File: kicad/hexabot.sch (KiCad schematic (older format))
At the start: 102 parts, among them P1 BATTERY, P10 BUMP2, P11 USB_B, P12 DEBUG, P13 NC, P14 MOTOR_R, P15 MOTOR_L, P16 UART1_5V, P17 ENC1, P18 ENC2, P19 ENC3, P2 EXT_POWER, P20 ENC4, P21 UART2_FTDI3V3, P22 NC, P23 START, P24 DYNAMIXEL2, P25 NC, P26 NC, P27 NC, P3 SERVO1, P4 SERVO2, P5 DYNAMIXEL1, P6 PICKIT, P7 PANIC BUTTON, P8 NC, P9 BUMP1, Q1 Q_NMOS_GSD, Q2 Q_NMOS_GSD, Q3 Q_NMOS_GSD, Q4 Q_NMOS_GSD, SW1 PUSH1, SW2 PUSH2, U1 PTN78020 +5V, U2 PTN78020 SERVO, U3 MCP1727, U4 DSPIC33EP256MU806, Y1 8M

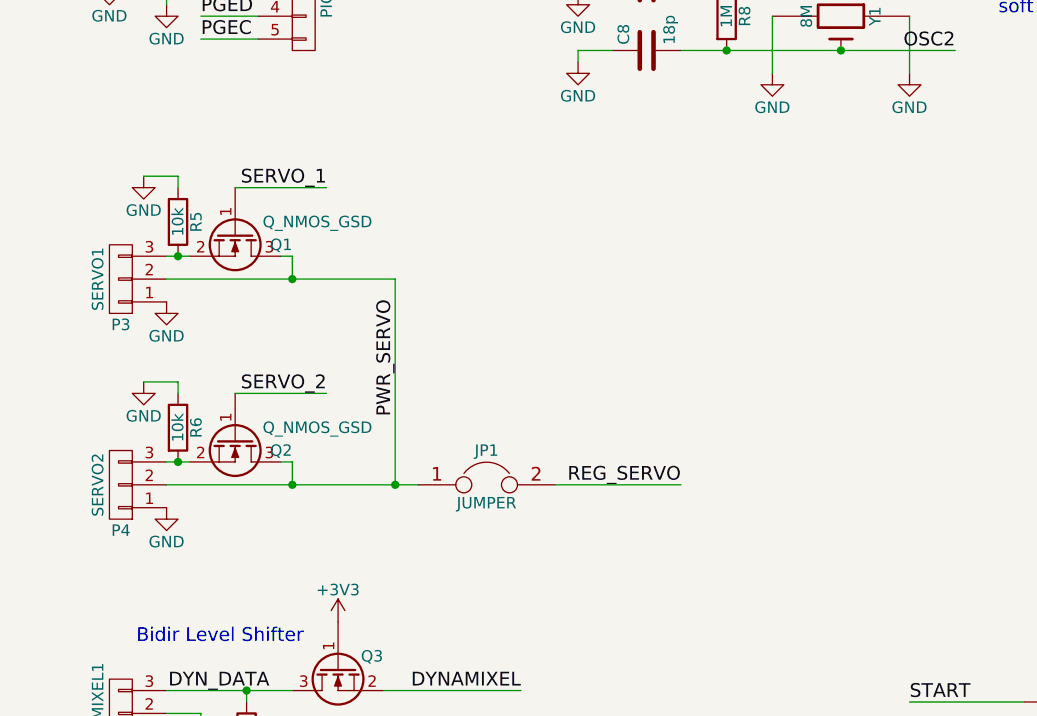
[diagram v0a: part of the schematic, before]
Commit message: Fix servo transistor in schematics, the netlist will have to change
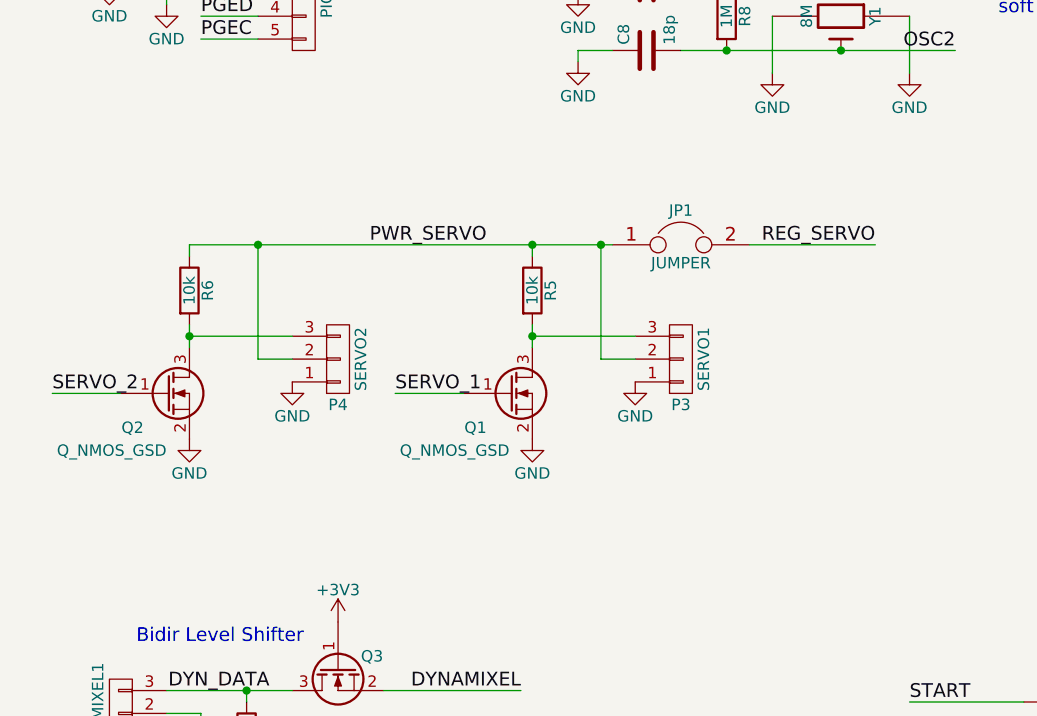
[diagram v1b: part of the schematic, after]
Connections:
- net GND: now also Q1.2 (S), Q2.2 (S); no longer R5.1, R6.1
- net PWR_SERVO: now also R5.1, R6.1; no longer Q1.3 (D), Q2.3 (D)
- net at P3.3 (P3), R5.2: now also Q1.3 (D); no longer Q1.2 (S)
- net at P4.3 (P3), R6.2: now also Q2.3 (D); no longer Q2.2 (S)
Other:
- moved on the sheet: JP1, P3, Q1, R5
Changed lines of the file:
@@
 L CONN_01X03 P3
 U 1 1 55780543
-P 1050 7150
-F 0 "P3" H 1050 7350 50  0000 C CNN
-F 1 "SERVO1" V 1150 7150 50  0000 C CNN
-F 2 "Pin_Headers:Pin_Header_Straight_1x03" H 1050 7150 60  0001 C CNN
-F 3 "" H 1050 7150 60  0000 C CNN
-	1    1050 7150
-	-1   0    0    1
-$EndComp
-Text Label 1950 6750 2    60   ~ 0
+P 3500 7500
+F 0 "P3" H 3500 7700 50  0000 C CNN
+F 1 "SERVO1" V 3600 7500 50  0000 C CNN
+F 2 "Pin_Headers:Pin_Header_Straight_1x03" H 3500 7500 60  0001 C CNN
+F 3 "" H 3500 7500 60  0000 C CNN
+	1    3500 7500
+	1    0    0    1
+$EndComp
+Text Label 2250 7650 0    60   ~ 0
 SERVO_1
 $Comp
 L GND #PWR017
 U 1 1 55781069
-P 1250 7250
-F 0 "#PWR017" H 1250 7000 50  0001 C CNN
-F 1 "GND" H 1250 7100 50  0000 C CNN
-F 2 "" H 1250 7250 60  0000 C CNN
-F 3 "" H 1250 7250 60  0000 C CNN
-	1    1250 7250
-	1    0    0    -1
+P 3300 7600
+F 0 "#PWR017" H 3300 7350 50  0001 C CNN
+F 1 "GND" H 3300 7450 50  0000 C CNN
+F 2 "" H 3300 7600 60  0000 C CNN
+F 3 "" H 3300 7600 60  0000 C CNN
+	1    3300 7600
+	-1   0    0    -1
 $EndComp
 $Comp
 L Q_NMOS_GSD Q1
 U 1 1 55782C1B
-P 1550 6950
-F 0 "Q1" V 1600 7200 50  0000 R CNN
-F 1 "Q_NMOS_GSD" V 1500 7550 50  0000 R CNN
-F 2 "Housings_SOT-23_SOT-143_TSOT-6:SOT-23" H 1750 7050 29  0001 C CNN
-F 3 "" H 1550 6950 60  0000 C CNN
-	1    1550 6950
-	0    1    1    0
+P 2750 7650
+F 0 "Q1" H 2650 7500 50  0000 R CNN
+F 1 "Q_NMOS_GSD" H 2750 7400 50  0000 R CNN
+F 2 "Housings_SOT-23_SOT-143_TSOT-6:SOT-23" H 2950 7750 29  0001 C CNN
+F 3 "" H 2750 7650 60  0000 C CNN
+	1    2750 7650
+	1    0    0    -1
 $EndComp
 Text Label 5750 4150 0    60   ~ 0
@@
 L JUMPER JP1
 U 1 1 55796F00
-P 2650 8050
-F 0 "JP1" H 2650 8200 50  0000 C CNN
-F 1 "JUMPER" H 2650 7970 50  0000 C CNN
-F 2 "Pin_Headers:Pin_Header_Straight_1x02" H 2650 8050 60  0001 C CNN
-F 3 "" H 2650 8050 60  0000 C CNN
-	1    2650 8050
+P 3500 7000
+F 0 "JP1" H 3500 7150 50  0000 C CNN
+F 1 "JUMPER" H 3500 6920 50  0000 C CNN
+F 2 "Pin_Headers:Pin_Header_Straight_1x02" H 3500 7000 60  0001 C CNN
+F 3 "" H 3500 7000 60  0000 C CNN
+	1    3500 7000
 	1    0    0    -1
 $EndComp
@@
 L R R5
 U 1 1 557C662F
-P 1300 6900
-F 0 "R5" V 1380 6900 50  0000 C CNN
-F 1 "10k" V 1300 6900 50  0000 C CNN
-F 2 "Resistors_SMD:R_0805" V 1230 6900 30  0001 C CNN
-F 3 "" H 1300 6900 30  0000 C CNN
-	1    1300 6900
+P 2850 7200
+F 0 "R5" V 2930 7200 50  0000 C CNN
+F 1 "10k" V 2850 7200 50  0000 C CNN
+F 2 "Resistors_SMD:R_0805" V 2780 7200 30  0001 C CNN
+F 3 "" H 2850 7200 30  0000 C CNN
+	1    2850 7200
 	1    0    0    -1
 $EndComp
@@
 L GND #PWR049
 U 1 1 557C668B
-P 1150 6700
-F 0 "#PWR049" H 1150 6450 50  0001 C CNN
-F 1 "GND" H 1150 6550 50  0000 C CNN
-F 2 "" H 1150 6700 60  0000 C CNN
-F 3 "" H 1150 6700 60  0000 C CNN
-	1    1150 6700
-	1    0    0    -1
-$EndComp
-$Comp
-L CONN_01X03 P4
-U 1 1 557C6E33
-P 1050 8050
-F 0 "P4" H 1050 8250 50  0000 C CNN
-F 1 "SERVO2" V 1150 8050 50  0000 C CNN
-F 2 "Pin_Headers:Pin_Header_Straight_1x03" H 1050 8050 60  0001 C CNN
-F 3 "" H 1050 8050 60  0000 C CNN
-	1    1050 8050
-	-1   0    0    1
-$EndComp
-Text Label 1950 7650 2    60   ~ 0
-SERVO_2
-$Comp
-L GND #PWR050
-U 1 1 557C6E3A
-P 1250 8150
-F 0 "#PWR050" H 1250 7900 50  0001 C CNN
-F 1 "GND" H 1250 8000 50  0000 C CNN
-F 2 "" H 1250 8150 60  0000 C CNN
-F 3 "" H 1250 8150 60  0000 C CNN
-	1    1250 8150
-	1    0    0    -1
-$EndComp
-$Comp
-L Q_NMOS_GSD Q2
-U 1 1 557C6E40
-P 1550 7850
-F 0 "Q2" V 1600 8100 50  0000 R CNN
-F 1 "Q_NMOS_GSD" V 1500 8450 50  0000 R CNN
-F 2 "Housings_SOT-23_SOT-143_TSOT-6:SOT-23" H 1750 7950 29  0001 C CNN
-F 3 "" H 1550 7850 60  0000 C CNN
-	1    1550 7850
-	0    1    1    0
-$EndComp
-$Comp
-L R R6
-U 1 1 557C6E4D
-P 1300 7800
-F 0 "R6" V 1380 7800 50  0000 C CNN
-F 1 "10k" V 1300 7800 50  0000 C CNN
-F 2 "Resistors_SMD:R_0805" V 1230 7800 30  0001 C CNN
-F 3 "" H 1300 7800 30  0000 C CNN
-	1    1300 7800
-	1    0    0    -1
-$EndComp
-$Comp
-L GND #PWR051
-U 1 1 557C6E53
-P 1150 7600
-F 0 "#PWR051" H 1150 7350 50  0001 C CNN
-F 1 "GND" H 1150 7450 50  0000 C CNN
-F 2 "" H 1150 7600 60  0000 C CNN
-F 3 "" H 1150 7600 60  0000 C CNN
-	1    1150 7600
+P 2850 7850
+F 0 "#PWR049" H 2850 7600 50  0001 C CNN
+F 1 "GND" H 2850 7700 50  0000 C CNN
+F 2 "" H 2850 7850 60  0000 C CNN
+F 3 "" H 2850 7850 60  0000 C CNN
+	1    2850 7850
 	1    0    0    -1
 $EndComp
@@
 Text Label 600  3400 0    60   ~ 0
 MOTOR_POWER
-Text Label 3500 8050 2    60   ~ 0
+Text Label 4350 7000 2    60   ~ 0
 REG_SERVO
-Text Label 2250 7750 1    60   ~ 0
+Text Label 2650 7000 2    60   ~ 0
 PWR_SERVO
 $Comp
@@
 	1250 9050 1400 9050
 Wire Wire Line
-	1300 7600 1300 7650
-Wire Wire Line
-	1150 7600 1300 7600
-Wire Wire Line
-	1250 7950 1350 7950
-Connection ~ 1800 8050
-Wire Wire Line
-	1800 7950 1800 8050
-Wire Wire Line
-	1750 7950 1800 7950
-Wire Wire Line
-	1550 7650 1950 7650
-Wire Wire Line
-	1300 6700 1300 6750
-Wire Wire Line
-	1150 6700 1300 6700
-Wire Wire Line
 	4450 2350 4700 2350
 Wire Wire Line
@@
 	5750 4150 6000 4150
 Wire Wire Line
-	1250 7050 1350 7050
-Wire Wire Line
-	1550 6750 1950 6750
-Wire Wire Line
 	3500 5850 4700 5850
 Wire Wire Line
@@
 Wire Wire Line
 	7550 3750 7550 3650
-Connection ~ 1300 7050
-Connection ~ 1300 7950
 Wire Wire Line
 	9750 5950 11000 5950
@@
 	1100 850  1100 900
 Wire Wire Line
-	3500 8050 2950 8050
-Wire Wire Line
-	1250 8050 2350 8050
-Wire Wire Line
-	1250 7150 2250 7150
+	4350 7000 3800 7000
 Wire Wire Line
 	3500 9350 2950 9350
-Wire Wire Line
-	2250 7150 2250 8050
-Wire Wire Line
-	1750 7050 1800 7050
-Wire Wire Line
-	1800 7050 1800 7150
-Connection ~ 1800 7150
-Connection ~ 2250 8050
 Wire Wire Line
 	1250 8950 1800 8950
@@
 Connection ~ 4200 5850
 Connection ~ 4200 6150
+Wire Wire Line
+	2850 7350 2850 7450
+Wire Wire Line
+	2850 7850 2850 7850
+Wire Wire Line
+	2850 7050 2850 7050
+Wire Wire Line
+	3300 7500 3150 7500
+Wire Wire Line
+	2850 7050 2850 7000
+Connection ~ 2850 7400
+$Comp
+L CONN_01X03 P4
+U 1 1 55B0E12F
+P 2000 7500
+F 0 "P4" H 2000 7700 50  0000 C CNN
+F 1 "SERVO2" V 2100 7500 50  0000 C CNN
+F 2 "Pin_Headers:Pin_Header_Straight_1x03" H 2000 7500 60  0001 C CNN
+F 3 "" H 2000 7500 60  0000 C CNN
+	1    2000 7500
+	1    0    0    1
+$EndComp
+$Comp
+L GND #PWR?
+U 1 1 55B0E136
+P 1800 7600
+F 0 "#PWR?" H 1800 7350 50  0001 C CNN
+F 1 "GND" H 1800 7450 50  0000 C CNN
+F 2 "" H 1800 7600 60  0000 C CNN
+F 3 "" H 1800 7600 60  0000 C CNN
+	1    1800 7600
+	-1   0    0    -1
+$EndComp
+$Comp
+L Q_NMOS_GSD Q2
+U 1 1 55B0E13C
+P 1250 7650
+F 0 "Q2" H 1150 7500 50  0000 R CNN
+F 1 "Q_NMOS_GSD" H 1250 7400 50  0000 R CNN
+F 2 "Housings_SOT-23_SOT-143_TSOT-6:SOT-23" H 1450 7750 29  0001 C CNN
+F 3 "" H 1250 7650 60  0000 C CNN
+	1    1250 7650
+	1    0    0    -1
+$EndComp
+$Comp
+L R R6
+U 1 1 55B0E142
+P 1350 7200
+F 0 "R6" V 1430 7200 50  0000 C CNN
+F 1 "10k" V 1350 7200 50  0000 C CNN
+F 2 "Resistors_SMD:R_0805" V 1280 7200 30  0001 C CNN
+F 3 "" H 1350 7200 30  0000 C CNN
+	1    1350 7200
+	1    0    0    -1
+$EndComp
+$Comp
+L GND #PWR?
+U 1 1 55B0E148
+P 1350 7850
+F 0 "#PWR?" H 1350 7600 50  0001 C CNN
+F 1 "GND" H 1350 7700 50  0000 C CNN
+F 2 "" H 1350 7850 60  0000 C CNN
+F 3 "" H 1350 7850 60  0000 C CNN
+	1    1350 7850
+	1    0    0    -1
+$EndComp
+Wire Wire Line
+	1350 7350 1350 7450
+Wire Wire Line
+	1350 7850 1350 7850
+Wire Wire Line
+	1350 7050 1350 7050
+Wire Wire Line
+	1800 7500 1650 7500
+Wire Wire Line
+	1350 7050 1350 7000
+Connection ~ 1350 7400
+Wire Wire Line
+	3300 7400 2850 7400
+Wire Wire Line
+	1350 7000 3200 7000
+Wire Wire Line
+	1350 7400 1800 7400
+Wire Wire Line
+	2250 7650 2550 7650
+Text Label 750  7650 0    60   ~ 0
+SERVO_2
+Wire Wire Line
+	750  7650 1050 7650
+Connection ~ 2850 7000
+Connection ~ 1650 7000
+Wire Wire Line
+	1650 7500 1650 7000
+Wire Wire Line
+	3150 7500 3150 7000
+Connection ~ 3150 7000
 $EndSCHEMATC
